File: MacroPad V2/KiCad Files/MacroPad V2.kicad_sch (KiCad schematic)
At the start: 15 parts, among them SW1 RotaryEncoder_Switch, SW2 RotaryEncoder_Switch, SW3 RotaryEncoder_Switch, U1 Pico

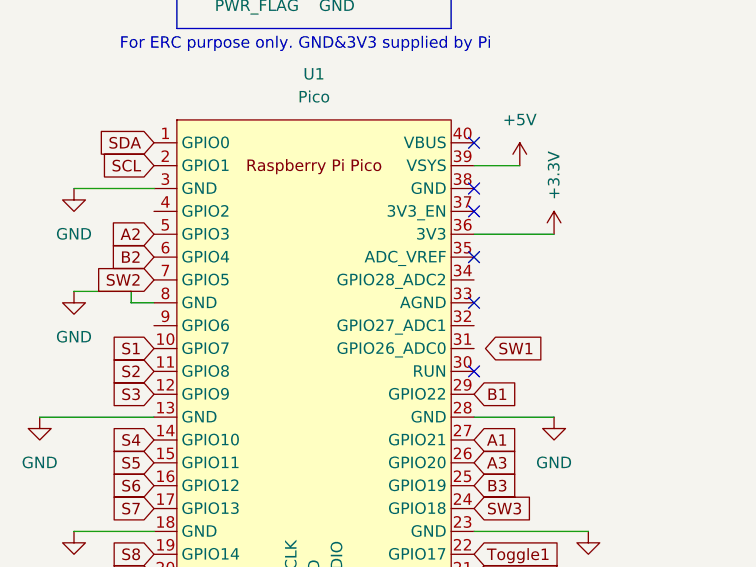
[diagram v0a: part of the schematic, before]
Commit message: Completed V2 and organised fiels
I rewired the PCB to avoid pins going through each other. YIPEE
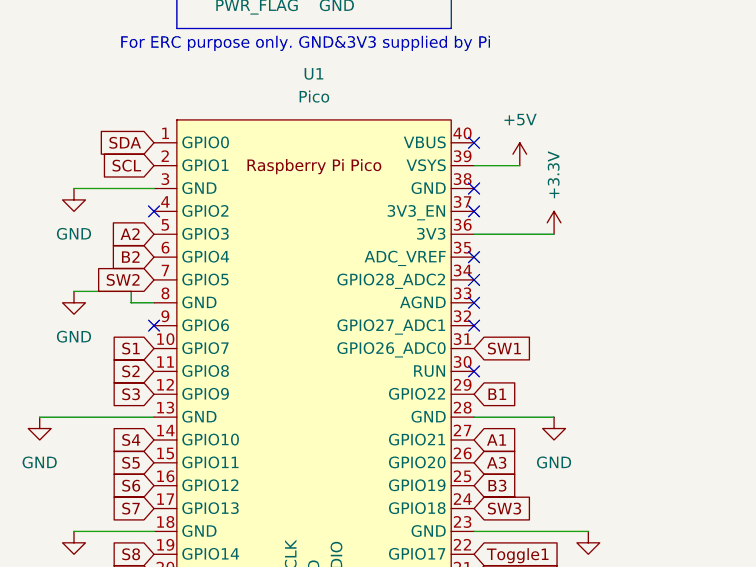
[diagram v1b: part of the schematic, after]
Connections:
- net SW1: now also U1.31 (GPIO26_ADC0)
- no-connect marks 8 -> 12
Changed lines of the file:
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@@
 (kicad_sch (version 20230121) (generator eeschema)
   (paper "A4")
+  (no_connect (at 80.01 67.31))
   (no_connect (at 80.01 64.77))
   (no_connect (at 80.01 69.85))
+  (no_connect (at 44.45 72.39))
   (no_connect (at 80.01 57.15))
   (no_connect (at 64.77 105.41))
@@
   (no_connect (at 80.01 52.07))
   (no_connect (at 80.01 59.69))
+  (no_connect (at 80.01 72.39))
+  (no_connect (at 44.45 59.69))
   (no_connect (at 80.01 77.47))
   (wire (pts (xy 222.25 118.11) (xy 217.17 118.11))
@@
     )
   )
-  (global_label "SW1" (shape input) (at 81.28 74.93 0) (fields_autoplaced)
-    (effects (font (size 1.27 1.27)) (justify left))
-    (property "Intersheetrefs" "${INTERSHEET_REFS}" (at 88.1356 74.93 0)
-      (effects (font (size 1.27 1.27)) (justify left) hide)
-    )
+  (global_label "SW1" (shape input) (at 80.01 74.93 0) (fields_autoplaced)
+    (effects (font (size 1.27 1.27)) (justify left))
+    (property "Intersheetrefs" "${INTERSHEET_REFS}" (at 86.8656 74.93 0)
+      (effects (font (size 1.27 1.27)) (justify left) hide)
+    )
